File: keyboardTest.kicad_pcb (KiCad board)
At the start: 2 copper layers, 294.2 x 101.2 mm, 118 parts, among them J1 DRAGON_CONNECTION, SW1 O, SW10 A, SW11 I, SW12 Q, SW13 Y, SW14 Clear, SW15 2, SW16 :, SW17 B, SW18 J, SW19 R, SW2 8, SW20 Z, SW21 Break, SW22 3, SW23 ;, SW24 C, SW25 K, SW26 S, SW27 Up, SW28 4, SW29 ,, SW3 At, SW30 D, SW31 L, SW32 T, SW33 Down, SW34 5, SW35 -, SW36 E, SW37 M, SW38 U, SW39 Left, SW4 H, SW40 6, SW41 ., SW42 F, SW43 N, SW44 V, SW45 Right, SW46 7, SW47 /, SW48 G, SW49 O, SW5 P, SW50 W, SW51 Space, SW52 Shift, SW53 Shift, SW6 X, SW7 Enter, SW8 1, SW9 9

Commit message: correct board dimensions
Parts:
- moved H2 10.0 mm to (353.3, 174.5)
- moved D3 0.51 mm to (288.1, 132.3)
- moved SW14 0.51 mm to (336.4, 152.2)
- moved D21 0.51 mm to (316.7, 112.7)
- moved D41 0.51 mm to (264.3, 170.3)
- moved SW1 0.51 mm to (264.9, 114.1)
- moved SW39 0.51 mm to (312.6, 133.1)
- moved SW47 0.51 mm to (288.7, 171.2)
- moved SW53 0.51 mm to (312.6, 171.2)
- moved D17 0.51 mm to (188.0, 170.3)
- moved D37 0.51 mm to (226.2, 170.3)
- moved D44 0.51 mm to (169.0, 170.3)
- moved D48 0.51 mm to (178.6, 151.3)
- moved SW18 0.51 mm to (222.1, 152.2)
- moved D28 0.51 mm to (145.2, 113.0)
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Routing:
- net PB2: track 394.4 -> 358.0 mm, vias 5 -> 4
- net PB6: track 339.1 -> 305.3 mm
- net PA4: track 301.0 -> 268.9 mm
- net PB3: track 307.0 -> 275.7 mm, vias 3 -> 4
- net PA5: track 406.6 -> 435.6 mm
- net PB1: track 371.5 -> 399.0 mm
- net PB0: track 340.8 -> 361.1 mm, vias 2 -> 3
- net PA1: track 319.6 -> 300.2 mm
- net PB7: track 466.0 -> 484.9 mm
- net PB4: track 261.5 -> 277.3 mm
- net PA3: track 242.8 -> 251.3 mm
- net PA2: track 307.0 -> 314.4 mm, vias 1 -> 0
- net PA6: track 381.8 -> 387.3 mm
- net Net-(D40-K): track 9.20 -> 3.79 mm
- net Net-(D21-K): track 9.30 -> 3.89 mm
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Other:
- board size 294.2 x 101.2 mm -> 304.2 x 101.2 mm

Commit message: rectify spacebar row
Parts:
- added D54: D, Diode_SMD:D_0805_2012Metric, B.Cu at (130.9, 188.3)
- added D55: D, Diode_SMD:D_0805_2012Metric, B.Cu at (264.3, 188.7)
- added SW54: Ctrl, Button_Switch_Keyboard:SW_Cherry_MX_1.00u_PCB, F.Cu at (136.3, 190.2)
- added SW55: Fn, Button_Switch_Keyboard:SW_Cherry_MX_1.00u_PCB, F.Cu at (269.7, 190.2)
- added SWS1: Switch Stabiliser, Mounting_Keyboard_Stabilizer:Stabilizer_Cherry_MX_6.00u, F.Cu at (200.4, 195.3)
- SW51: footprint Button_Switch_Keyboard:SW_Cherry_MX_6.25u_PCB -> Switch_Keyboard_Cherry_MX:SW_Cherry_MX_PCB_6.00u
- moved H10 17.4 mm to (189.4, 201.3)
- moved SW51 5.69 mm to (200.4, 195.3)
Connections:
- SW51 pad 1: PA5 -> Net-(D51-K)
- SW51 pad 2: Net-(D51-K) -> PA5
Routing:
- net PA6: track 387.3 -> 489.3 mm
- net PB3: track 275.7 -> 305.3 mm, vias 4 -> 6
- net PB6: track 305.3 -> 321.8 mm, vias 1 -> 3
- net Net-(D54-K): track 0.00 -> 4.45 mm
- net Net-(D55-K): track 0.00 -> 4.06 mm
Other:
- outline, holes or cut-outs redrawn

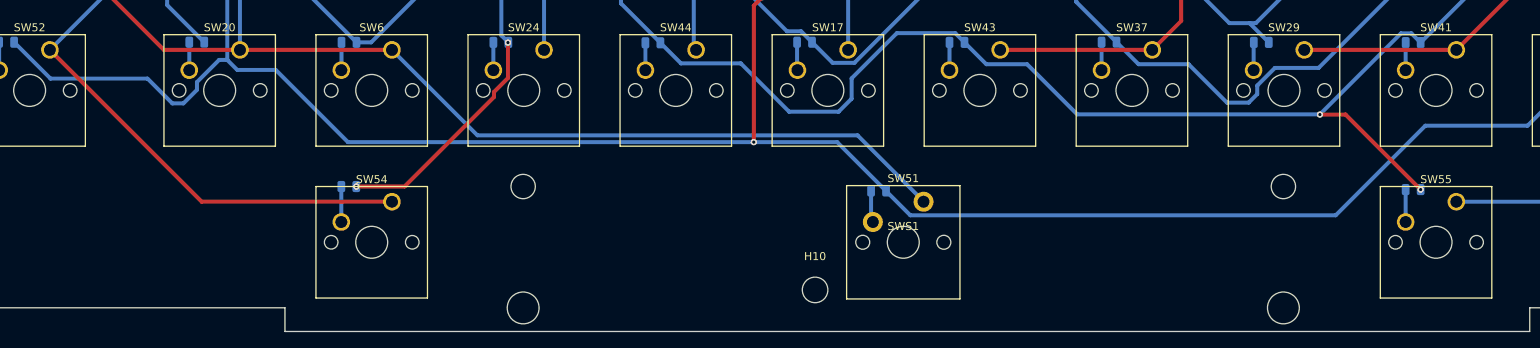
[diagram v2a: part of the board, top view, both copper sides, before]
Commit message: update pcb for spare stabiliser position
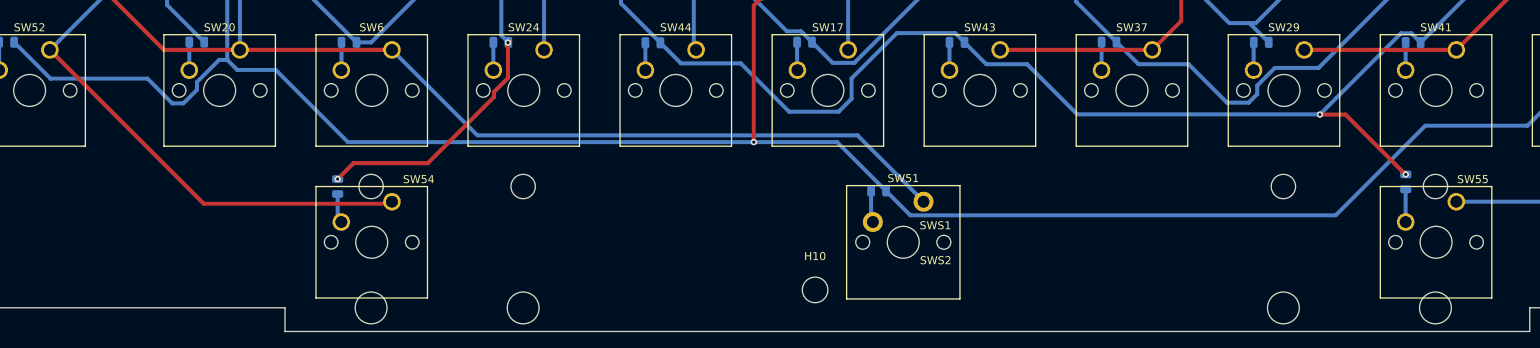
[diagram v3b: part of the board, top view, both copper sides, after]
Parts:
- added SWS2: 8u Switch Stabiliser, Mounting_Keyboard_Stabilizer:Stabilizer_Cherry_MX_8.00u, F.Cu at (200.4, 195.3)
- SWS1: value Switch Stabiliser -> 6u Switch Stabiliser
- moved D54 1.40 mm to (129.5, 188.3), turned to 90 degrees
- moved D55 1.33 mm to (263.4, 187.8), turned to 90 degrees
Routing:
- net PB6: track 321.8 -> 319.2 mm
- net PB3: track 305.3 -> 307.2 mm
- net Net-(D54-K): track 4.45 -> 3.70 mm

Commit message: revise board dimensions
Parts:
- moved H2 5.31 mm to (348.0, 174.5)
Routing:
- net PB0: track 361.1 -> 361.9 mm
- net PB1: track 399.0 -> 399.6 mm
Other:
- board size 304.2 x 101.2 mm -> 298.8 x 101.2 mm

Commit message: shrinkify board
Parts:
- removed H1, H2: MountingHole, MountingHole:MountingHole_5.3mm_M5
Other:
- board size 298.8 x 101.2 mm -> 273.3 x 101.2 mm
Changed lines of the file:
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@@
     (property "Sheetfile" "keyboardTest.kicad_sch")
     (property "Sheetname" "")
+    (property "dnp" "")
+    (property "exclude_from_bom" "")
     (property "ki_description" "Mounting Hole without connection")
     (property "ki_keywords" "mounting hole")
-    (attr exclude_from_pos_files)
+    (attr exclude_from_pos_files exclude_from_bom)
     (fp_text reference "H5" (at 0 -4.2) (layer "F.SilkS")
         (effects (font (size 1 1) (thickness 0.15)))
@@
     )
   )
-  (footprint "MountingHole:MountingHole_5.3mm_M5" locked (layer "F.Cu")
-    (at 65.3796 154.432)
-    (descr "Mounting Hole 5.3mm, no annular, M5")
-    (tags "mounting hole 5.3mm no annular m5")
-    (property "Sheetfile" "keyboardTest.kicad_sch")
-    (property "Sheetname" "")
-    (property "ki_description" "Mounting Hole without connection")
-    (property "ki_keywords" "mounting hole")
-    (attr exclude_from_pos_files)
-    (fp_text reference "H1" (at 0 -6.3) (layer "F.SilkS")
-        (effects (font (size 1 1) (thickness 0.15)))
-    )
-    (fp_text value "MountingHole" (at 0 6.3) (layer "F.Fab")
-        (effects (font (size 1 1) (thickness 0.15)))
-    )
-    (fp_text user "${REFERENCE}" (at 0 0) (layer "F.Fab")
-        (effects (font (size 1 1) (thickness 0.15)))
-    )
-    (fp_circle (center 0 0) (end 5.3 0)
-      (stroke (width 0.15) (type solid)) (fill none) (layer "Cmts.User"))
-    (fp_circle (center 0 0) (end 5.55 0)
-      (stroke (width 0.05) (type solid)) (fill none) (layer "F.CrtYd"))
-    (pad "" np_thru_hole circle locked (at 0 0) (size 5.3 5.3) (drill 5.3) (layers "*.Cu" "*.Mask"))
-  )
   (footprint "Button_Switch_Keyboard:SW_Cherry_MX_1.00u_PCB" (layer "F.Cu")
     (at 198.2597 133.1214)
@@
     (property "Sheetfile" "keyboardTest.kicad_sch")
     (property "Sheetname" "")
+    (property "dnp" "")
+    (property "exclude_from_bom" "")
     (property "ki_description" "Mounting Hole without connection")
     (property "ki_keywords" "mounting hole")
-    (attr exclude_from_pos_files)
+    (attr exclude_from_pos_files exclude_from_bom)
     (fp_text reference "H10" (at 0 -4.2) (layer "F.SilkS")
         (effects (font (size 1 1) (thickness 0.15)))
@@
     )
   )
-  (footprint "MountingHole:MountingHole_5.3mm_M5" (layer "F.Cu")
-    (at 348 174.4726)
-    (descr "Mounting Hole 5.3mm, no annular, M5")
-    (tags "mounting hole 5.3mm no annular m5")
-    (property "Sheetfile" "keyboardTest.kicad_sch")
-    (property "Sheetname" "")
-    (property "ki_description" "Mounting Hole without connection")
-    (property "ki_keywords" "mounting hole")
-    (attr exclude_from_pos_files)
-    (fp_text reference "H2" (at 0 -6.3) (layer "F.SilkS")
-        (effects (font (size 1 1) (thickness 0.15)))
-    )
-    (fp_text value "MountingHole" (at 0 6.3) (layer "F.Fab")
-        (effects (font (size 1 1) (thickness 0.15)))
-    )
-    (fp_text user "${REFERENCE}" (at 0 0) (layer "F.Fab")
-        (effects (font (size 1 1) (thickness 0.15)))
-    )
-    (fp_circle (center 0 0) (end 5.3 0)
-      (stroke (width 0.15) (type solid)) (fill none) (layer "Cmts.User"))
-    (fp_circle (center 0 0) (end 5.55 0)
-      (stroke (width 0.05) (type solid)) (fill none) (layer "F.CrtYd"))
-    (pad "" np_thru_hole circle (at 0 0) (size 5.3 5.3) (drill 5.3) (layers "*.Cu" "*.Mask"))
-  )
   (footprint "Button_Switch_Keyboard:SW_Cherry_MX_1.00u_PCB" (layer "F.Cu")
     (at 83.9597 133.1214)
@@
     (property "Sheetfile" "keyboardTest.kicad_sch")
     (property "Sheetname" "")
+    (property "dnp" "")
+    (property "exclude_from_bom" "")
     (property "ki_description" "Mounting Hole without connection")
     (property "ki_keywords" "mounting hole")
-    (attr exclude_from_pos_files)
+    (attr exclude_from_pos_files exclude_from_bom)
     (fp_text reference "H7" (at 0 -4.2) (layer "F.SilkS")
         (effects (font (size 1 1) (thickness 0.15)))
@@
     (property "Sheetfile" "keyboardTest.kicad_sch")
     (property "Sheetname" "")
+    (property "dnp" "")
+    (property "exclude_from_bom" "")
     (property "ki_description" "Mounting Hole without connection")
     (property "ki_keywords" "mounting hole")
-    (attr exclude_from_pos_files)
+    (attr exclude_from_pos_files exclude_from_bom)
     (fp_text reference "H9" (at 0 -4.2) (layer "F.SilkS")
         (effects (font (size 1 1) (thickness 0.15)))
@@
     (property "Sheetfile" "keyboardTest.kicad_sch")
     (property "Sheetname" "")
+    (property "dnp" "")
+    (property "exclude_from_bom" "")
     (property "ki_description" "Mounting Hole without connection")
     (property "ki_keywords" "mounting hole")
-    (attr exclude_from_pos_files)
+    (attr exclude_from_pos_files exclude_from_bom)
     (fp_text reference "H11" (at 0 -4.2) (layer "F.SilkS")
         (effects (font (size 1 1) (thickness 0.15)))
@@
     (property "Sheetfile" "keyboardTest.kicad_sch")
     (property "Sheetname" "")
+    (property "dnp" "")
+    (property "exclude_from_bom" "")
     (property "ki_description" "Mounting Hole without connection")
     (property "ki_keywords" "mounting hole")
-    (attr exclude_from_pos_files)
+    (attr exclude_from_pos_files exclude_from_bom)
     (fp_text reference "H6" (at 0 -4.2) (layer "F.SilkS")
         (effects (font (size 1 1) (thickness 0.15)))
@@
     (property "Sheetfile" "keyboardTest.kicad_sch")
     (property "Sheetname" "")
+    (property "dnp" "")
+    (property "exclude_from_bom" "")
     (property "ki_description" "Mounting Hole without connection")
     (property "ki_keywords" "mounting hole")
-    (attr exclude_from_pos_files)
+    (attr exclude_from_pos_files exclude_from_bom)
     (fp_text reference "H3" (at 0 -4.2) (layer "F.SilkS")
         (effects (font (size 1 1) (thickness 0.15)))
@@
     (property "Sheetfile" "keyboardTest.kicad_sch")
     (property "Sheetname" "")
+    (property "dnp" "")
+    (property "exclude_from_bom" "")
     (property "ki_description" "Mounting Hole without connection")
     (property "ki_keywords" "mounting hole")
-    (attr exclude_from_pos_files)
+    (attr exclude_from_pos_files exclude_from_bom)
     (fp_text reference "H4" (at 0 -4.2) (layer "F.SilkS")
         (effects (font (size 1 1) (thickness 0.15)))
@@
     (property "Sheetfile" "keyboardTest.kicad_sch")
     (property "Sheetname" "")
+    (property "dnp" "")
+    (property "exclude_from_bom" "")
     (property "ki_description" "Mounting Hole without connection")
     (property "ki_keywords" "mounting hole")
-    (attr exclude_from_pos_files)
+    (attr exclude_from_pos_files exclude_from_bom)
     (fp_text reference "H8" (at 0 -4.2) (layer "F.SilkS")
         (effects (font (size 1 1) (thickness 0.15)))
@@
     )
   )
-  (gr_arc (start 356.1 203.3016) (mid 356.033045 203.463245) (end 355.8714 203.5302)
+  (gr_arc (start 344.398888 203.3016) (mid 344.331933 203.463245) (end 344.170288 203.5302)
     (stroke (width 0.1) (type default)) (layer "Edge.Cuts"))
   (gr_line (start 122.936 206.502) (end 121.158 203.5302)
     (stroke (width 0.1) (type default)) (layer "Edge.Cuts"))
-  (gr_line (start 57.2516 203.292355) (end 57.2516 105.537)
+  (gr_line (start 71.1454 203.291792) (end 71.1454 105.536437)
     (stroke (width 0.1) (type default)) (layer "Edge.Cuts"))
   (gr_line (start 278.892 206.502) (end 122.936 206.502)
     (stroke (width 0.1) (type default)) (layer "Edge.Cuts"))
-  (gr_line (start 121.158 203.5302) (end 57.4802 203.5302)
+  (gr_line (start 121.158 203.5302) (end 71.374 203.529637)
     (stroke (width 0.1) (type default)) (layer "Edge.Cuts"))
-  (gr_arc (start 355.871112 105.307837) (mid 356.032757 105.374792) (end 356.099712 105.536437)
+  (gr_arc (start 344.17 105.307837) (mid 344.331624 105.374799) (end 344.3986 105.536437)
     (stroke (width 0.1) (type default)) (layer "Edge.Cuts"))
-  (gr_arc (start 57.2516 105.537) (mid 57.318555 105.375355) (end 57.4802 105.3084)
+  (gr_arc (start 71.1454 105.536437) (mid 71.212355 105.374792) (end 71.374 105.307837)
     (stroke (width 0.1) (type default)) (layer "Edge.Cuts"))
-  (gr_line (start 356.099712 105.536437) (end 356.1 203.3016)
+  (gr_line (start 344.3986 105.536437) (end 344.398888 203.3016)
     (stroke (width 0.1) (type default)) (layer "Edge.Cuts"))
-  (gr_arc (start 57.4802 203.5302) (mid 57.31664 203.458623) (end 57.2516 203.292355)
+  (gr_arc (start 71.374 203.529637) (mid 71.210434 203.458065) (end 71.1454 203.291792)
     (stroke (width 0.1) (type default)) (layer "Edge.Cuts"))
-  (gr_line (start 355.8714 203.5302) (end 280.162 203.5302)
+  (gr_line (start 344.170288 203.5302) (end 280.162 203.5302)
     (stroke (width 0.1) (type default)) (layer "Edge.Cuts"))
   (gr_line (start 280.162 203.5302) (end 278.892 206.502)
     (stroke (width 0.1) (type default)) (layer "Edge.Cuts"))
-  (gr_line (start 57.4802 105.3084) (end 355.871112 105.307837)
+  (gr_line (start 71.374 105.307837) (end 344.17 105.307837)
     (stroke (width 0.1) (type default)) (layer "Edge.Cuts"))
   (gr_line (start 351.4344 174.4472) (end 346.0242 174.4472)
@@
   (gr_line (start 57.2516 154.4066) (end 62.6618 154.4066)
     (stroke (width 0.15) (type default)) (layer "User.8"))
-  (gr_line (start 356.660644 203.568284) (end 356.660644 105.295684)
+  (gr_line (start 344.424 203.568284) (end 344.424 105.295684)
     (stroke (width 0.15) (type default)) (layer "User.8"))
   (gr_line (start 71.247 105.3084) (end 71.247 203.5048)
